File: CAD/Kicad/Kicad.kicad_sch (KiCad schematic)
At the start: 34 parts, among them J1 USB_C_Receptacle_USB2.0_14P, Q1 2N3904, Q2 2N3904, SW1 SW_Push, SW2 SW_Push, U1 ESP32-S3-WROOM-2, U2 TLV75533PDRV, U8 MPU-9250, U9 FT231XQ

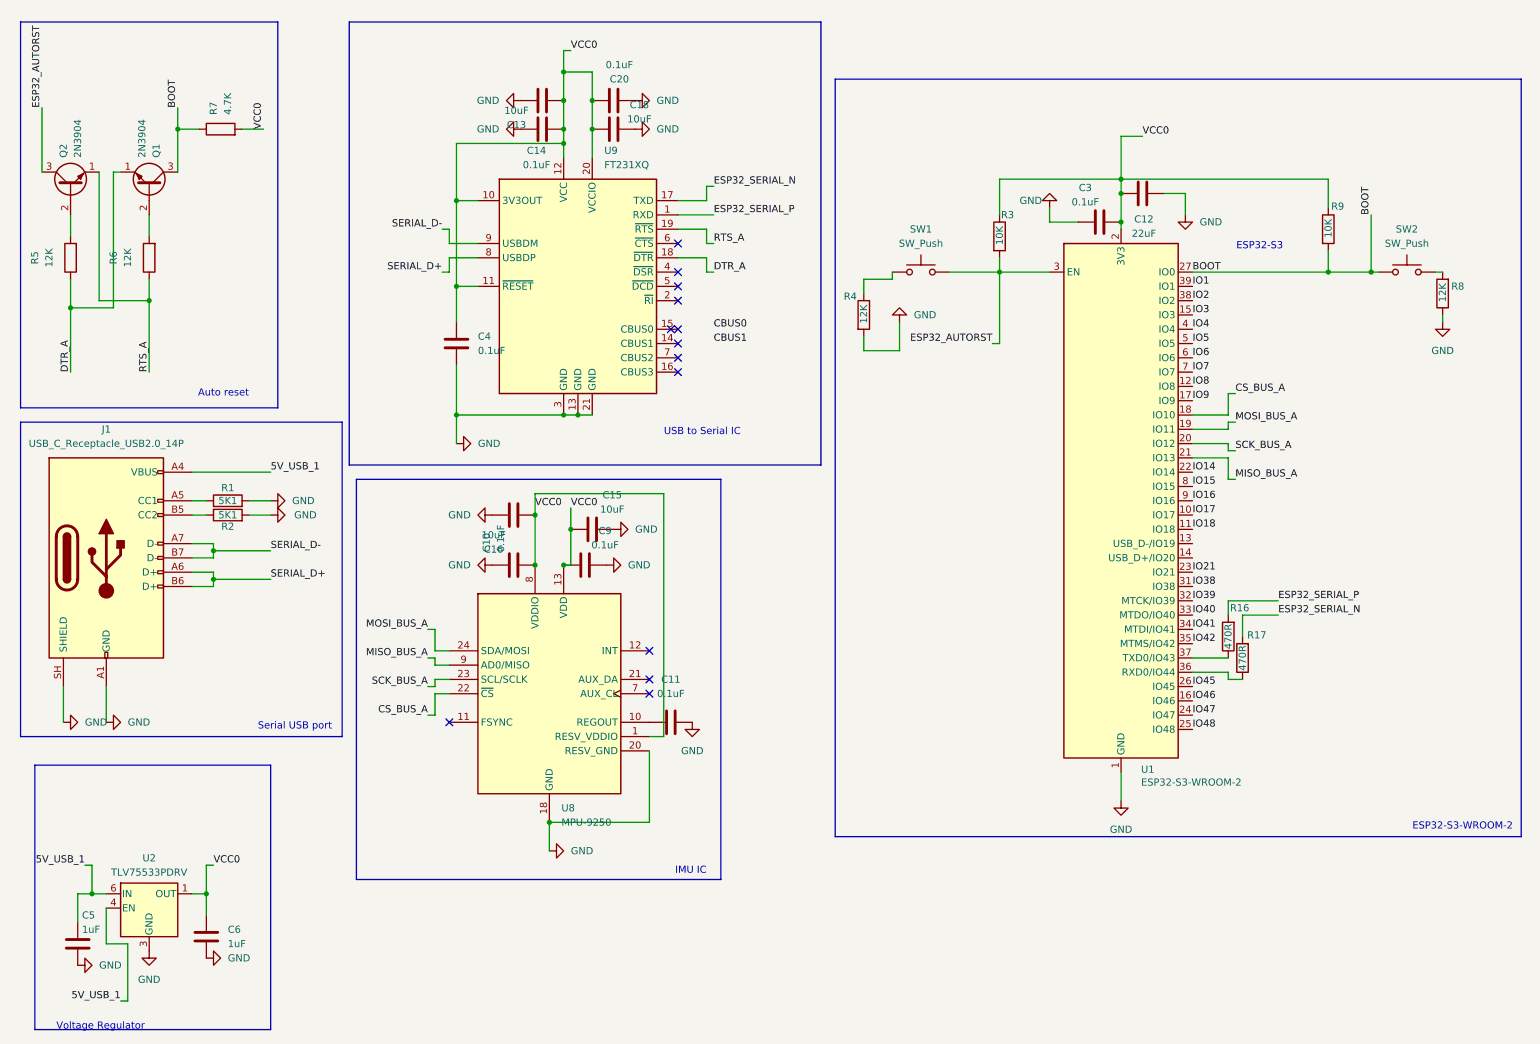
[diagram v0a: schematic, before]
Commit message: redid BOM and replaced FT231XQ
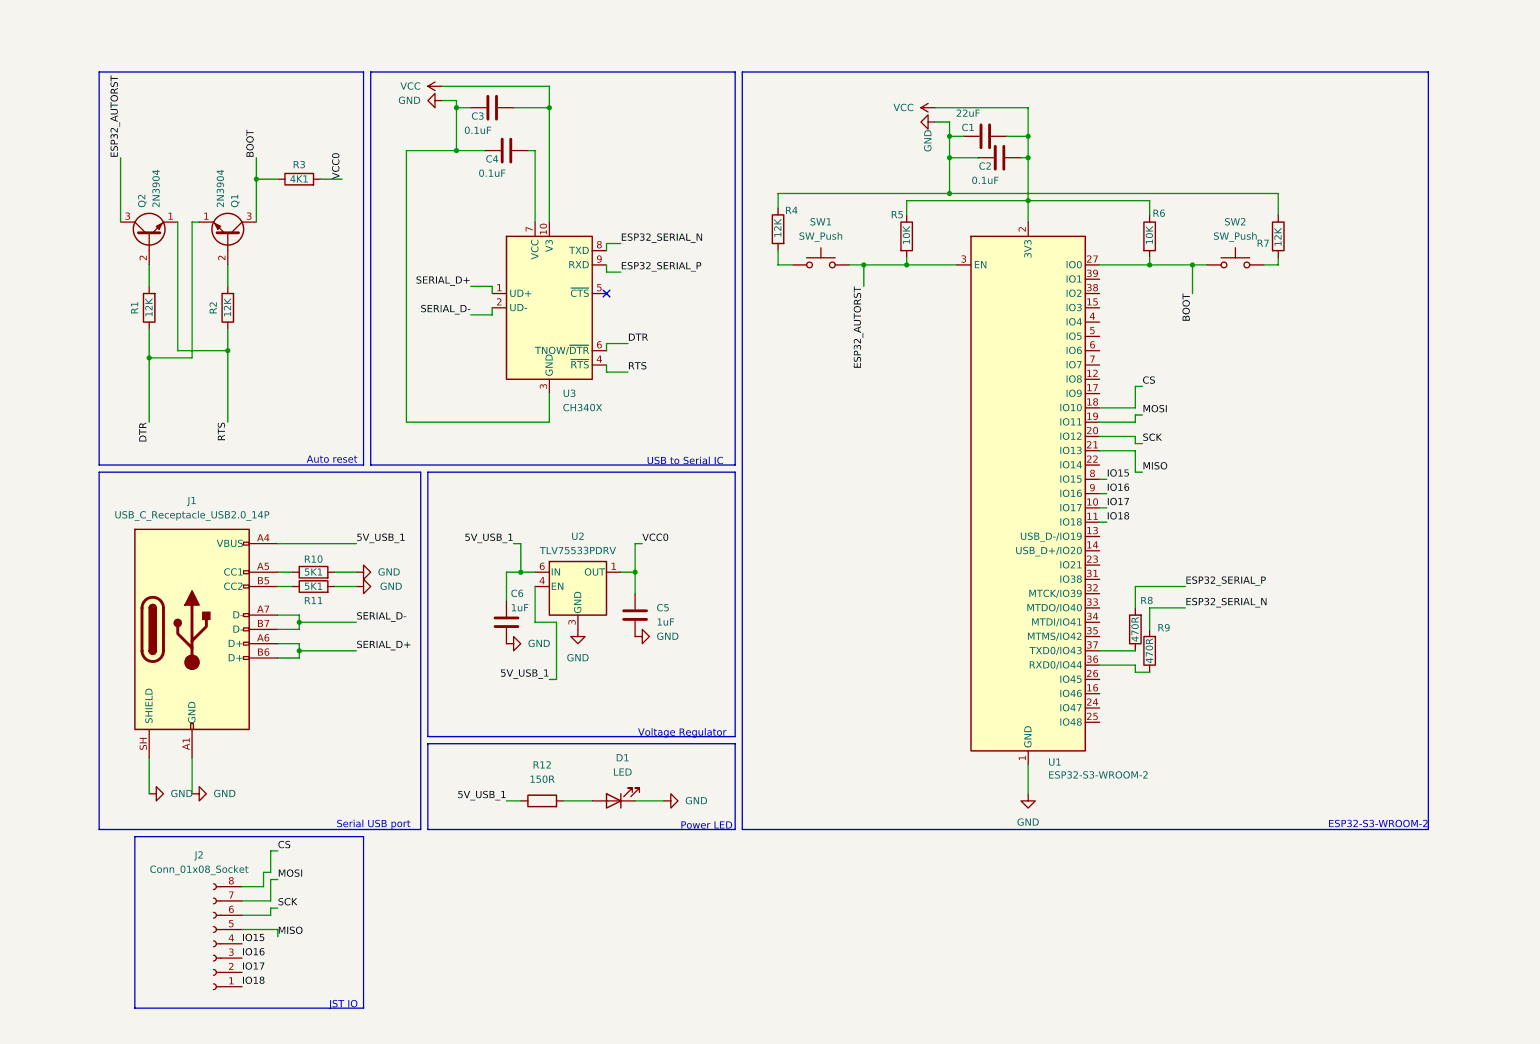
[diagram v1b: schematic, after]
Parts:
- removed C10, C14, C20, C9: 0.1uF, Capacitor_SMD:C_01005_0402Metric, symbol Device:C
- removed C11: 0.1uF, Capacitor_SMD:C_0201_0603Metric, symbol Device:C
- removed C13, C15, C16, C18: 10uF, Capacitor_SMD:C_01005_0402Metric, symbol Device:C
- removed U8: MPU-9250, Sensor_Motion:InvenSense_QFN-24_3x3mm_P0.4mm, symbol Sensor_Motion:MPU-9250
- removed U9: FT231XQ, Package_DFN_QFN:QFN-20-1EP_4x4mm_P0.5mm_EP2.5x2.5mm, symbol Interface_USB:FT231XQ
- added C3: 0.1uF, Capacitor_SMD:C_01005_0402Metric, symbol Device:C
- added D1: LED, LED_SMD:LED_0201_0603Metric, symbol Device:LED
- added J2: Conn_01x08_Socket, Connector_JST:JST_EH_S8B-EH_1x08_P2.50mm_Horizontal, symbol Connector:Conn_01x08_Socket
- added R12: 150R, Resistor_SMD:R_01005_0402Metric, symbol Device:R
- added U3: CH340X, Package_SO:MSOP-10_3x3mm_P0.5mm, symbol Interface_USB:CH340X
- C5: renamed from C6; LCSC Part # C14445 -> C52923
- C6: renamed from C5; LCSC Part # C14445 -> C52923
- R1: renamed from R5; LCSC Part # C177293 -> C25752
- R10: renamed from R1; LCSC Part # C177348 -> C25905
- R2: renamed from R6; LCSC Part # C177293 -> C25752
- R3: renamed from R7; value 4.7K -> 4K1; LCSC Part # C22356632 -> C4109
- R4: LCSC Part # C177293 -> C25752
- R5: renamed from R3; LCSC Part # C177337 -> C4109
- R6: renamed from R9; LCSC Part # C177337 -> C4109
- R7: renamed from R8; LCSC Part # C177293 -> C25752
- renumbered C12 to C1, C3 to C2, R2 to R11, R16 to R8, R17 to R9
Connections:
- net 5V_USB_1: now also R12.1
- net ESP32_SERIAL_N: now also U3.8 (TXD)
- net ESP32_SERIAL_P: now also U3.9 (RXD)
- net GND: now also C4.1, R4.1, C3.1, D1.1 (K), U3.3 (GND); no longer C4.2, R4.2
- net IO15: now also J2.4 (Pin_4)
- net IO16: now also J2.3 (Pin_3)
- net IO17: now also J2.2 (Pin_2)
- net IO18: now also J2.1 (Pin_1)
- net SERIAL_D+: now also U3.1 (UD+)
- net SERIAL_D-: now also U3.2 (UD-)
- net VCC0: no longer C1.1, C2.2, C4.1, R5.1, R6.1, U1.2 (3V3)
- net at SW1.1: now also R4.2; no longer R4.1
- net CS_BUS_A renamed CS
- net CS: now also J2.8 (Pin_8)
- net DTR_A renamed DTR
- net DTR: now also U3.6 (TNOW/~{DTR})
- net IO1: no longer names the net of U1.39 (IO1)
- net IO14: no longer names the net of U1.22 (IO14)
- net IO2: no longer names the net of U1.38 (IO2)
- net IO21: no longer names the net of U1.23 (IO21)
- net IO3: no longer names the net of U1.15 (IO3)
- net IO38: no longer names the net of U1.31 (IO38)
- net IO39: no longer names the net of U1.32 (MTCK/IO39)
- net IO4: no longer names the net of U1.4 (IO4)
- net IO40: no longer names the net of U1.33 (MTDO/IO40)
- net IO41: no longer names the net of U1.34 (MTDI/IO41)
- net IO42: no longer names the net of U1.35 (MTMS/IO42)
- net IO45: no longer names the net of U1.26 (IO45)
- net IO46: no longer names the net of U1.16 (IO46)
- net IO47: no longer names the net of U1.24 (IO47)
- net IO48: no longer names the net of U1.25 (IO48)
- net IO5: no longer names the net of U1.5 (IO5)
- net IO6: no longer names the net of U1.6 (IO6)
- net IO7: no longer names the net of U1.7 (IO7)
- net IO8: no longer names the net of U1.12 (IO8)
- net IO9: no longer names the net of U1.17 (IO9)
- net MISO_BUS_A renamed MISO
- net MISO: now also J2.5 (Pin_5)
- net MOSI_BUS_A renamed MOSI
- net MOSI: now also J2.7 (Pin_7)
- net RTS_A renamed RTS
- net RTS: now also U3.4 (~{RTS})
- net SCK_BUS_A renamed SCK
- net SCK: now also J2.6 (Pin_6)
- new net: D1.2 (A), R12.2
- new net: C4.2, U3.7 (VCC)
- new net VCC: C1.1, C2.2, C3.2, R5.1, R6.1, U1.2 (3V3), U3.10 (V3)
- no-connect marks 13 -> 1
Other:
- note added: "JST IO"
- note added: "Power LED"
- note removed: "ESP32-S3"
- note removed: "IMU IC"
- moved on the sheet: C1, C2, C5, C6, J1, Q1, Q2, R1, R10, R11, R2, R3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

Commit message: finished rev4
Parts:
- removed Q1, Q2: 2N3904, Package_TO_SOT_THT:TO-92Flat, symbol Transistor_BJT:2N3904
- added Q3, Q4: MMBT3904, Package_TO_SOT_SMD:SOT-23, symbol Transistor_BJT:MMBT3904
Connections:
- net VCC0 is gone; now on net VCC: C5.1, R3.2, U2.1 (OUT)
- net BOOT: now also Q4.3 (C)
- net CS: now also J2.4 (Pin_4); no longer J2.8 (Pin_8)
- net DTR: now also Q4.2 (E)
- net ESP32_AUTORST: now also Q3.3 (C)
- net IO15: now also J2.8 (Pin_8); no longer J2.4 (Pin_4)
- net IO16: now also J2.7 (Pin_7); no longer J2.3 (Pin_3)
- net IO17: now also J2.6 (Pin_6); no longer J2.2 (Pin_2)
- net IO18: now also J2.5 (Pin_5); no longer J2.1 (Pin_1)
- net MISO: now also J2.1 (Pin_1); no longer J2.5 (Pin_5)
- net MOSI: now also J2.3 (Pin_3); no longer J2.7 (Pin_7)
- net RTS: now also Q3.2 (E)
- net SCK: now also J2.2 (Pin_2); no longer J2.6 (Pin_6)
- net at R2.2: now also Q4.1 (B)
- net at R1.2: now also Q3.1 (B)
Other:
- moved on the sheet: R3

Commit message: fixed BOM and markdown typo
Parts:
- R12: value 150R -> 200R; LCSC Part # C4109 -> C25087
- R5, R6: LCSC Part # C4109 -> C131361
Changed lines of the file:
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@@
 			)
 		)
-		(property "LCSC Part #" "C4109"
+		(property "LCSC Part #" "C131361"
 			(at 173.99 53.34 0)
 			(hide yes)
@@
 			)
 		)
-		(property "Value" "150R"
+		(property "Value" "200R"
 			(at 109.22 149.86 90)
 			(show_name no)
@@
 			)
 		)
-		(property "LCSC Part #" "C4109"
+		(property "LCSC Part #" "C25087"
 			(at 109.22 153.67 90)
 			(hide yes)
@@
 			)
 		)
-		(property "LCSC Part #" "C4109"
+		(property "LCSC Part #" "C131361"
 			(at 217.17 53.34 0)
 			(hide yes)
